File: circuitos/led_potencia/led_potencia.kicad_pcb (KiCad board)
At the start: 2 copper layers, 88.7 x 115.2 mm, 67 parts, among them J1 Conn_01x02_Pin, J10 Conn_01x02_Pin, J11 Conn_01x02_Pin, J12 Conn_01x02_Pin, J13 Conn_01x02_Pin, J14 Conn_01x02_Pin, J15 Conn_01x02_Pin, J16 Conn_01x02_Pin, J17 Conn_01x02_Socket, J19 Conn_01x02_OE_GND, J2 Conn_01x02_Pin, J20 Conn_01x05_IN, J21 Conn_01x05_OUT, J3 Conn_01x02_Pin, J4 Conn_01x02_Pin, J5 Conn_01x02_Pin, J6 Conn_01x02_Pin, J7 Conn_01x02_Pin, J8 Conn_01x02_Pin, J9 Conn_01x02_Pin, Q1 IRLZ44N, Q18 IRF4905, Q19 IRF4905, Q2 IRLZ44N, Q20 IRF4905, Q21 PN2222A, Q22 PN2222A, Q23 PN2222A, Q24 IRF4905, Q25 PN2222A, Q3 IRLZ44N, Q4 IRLZ44N, U1 74HC595

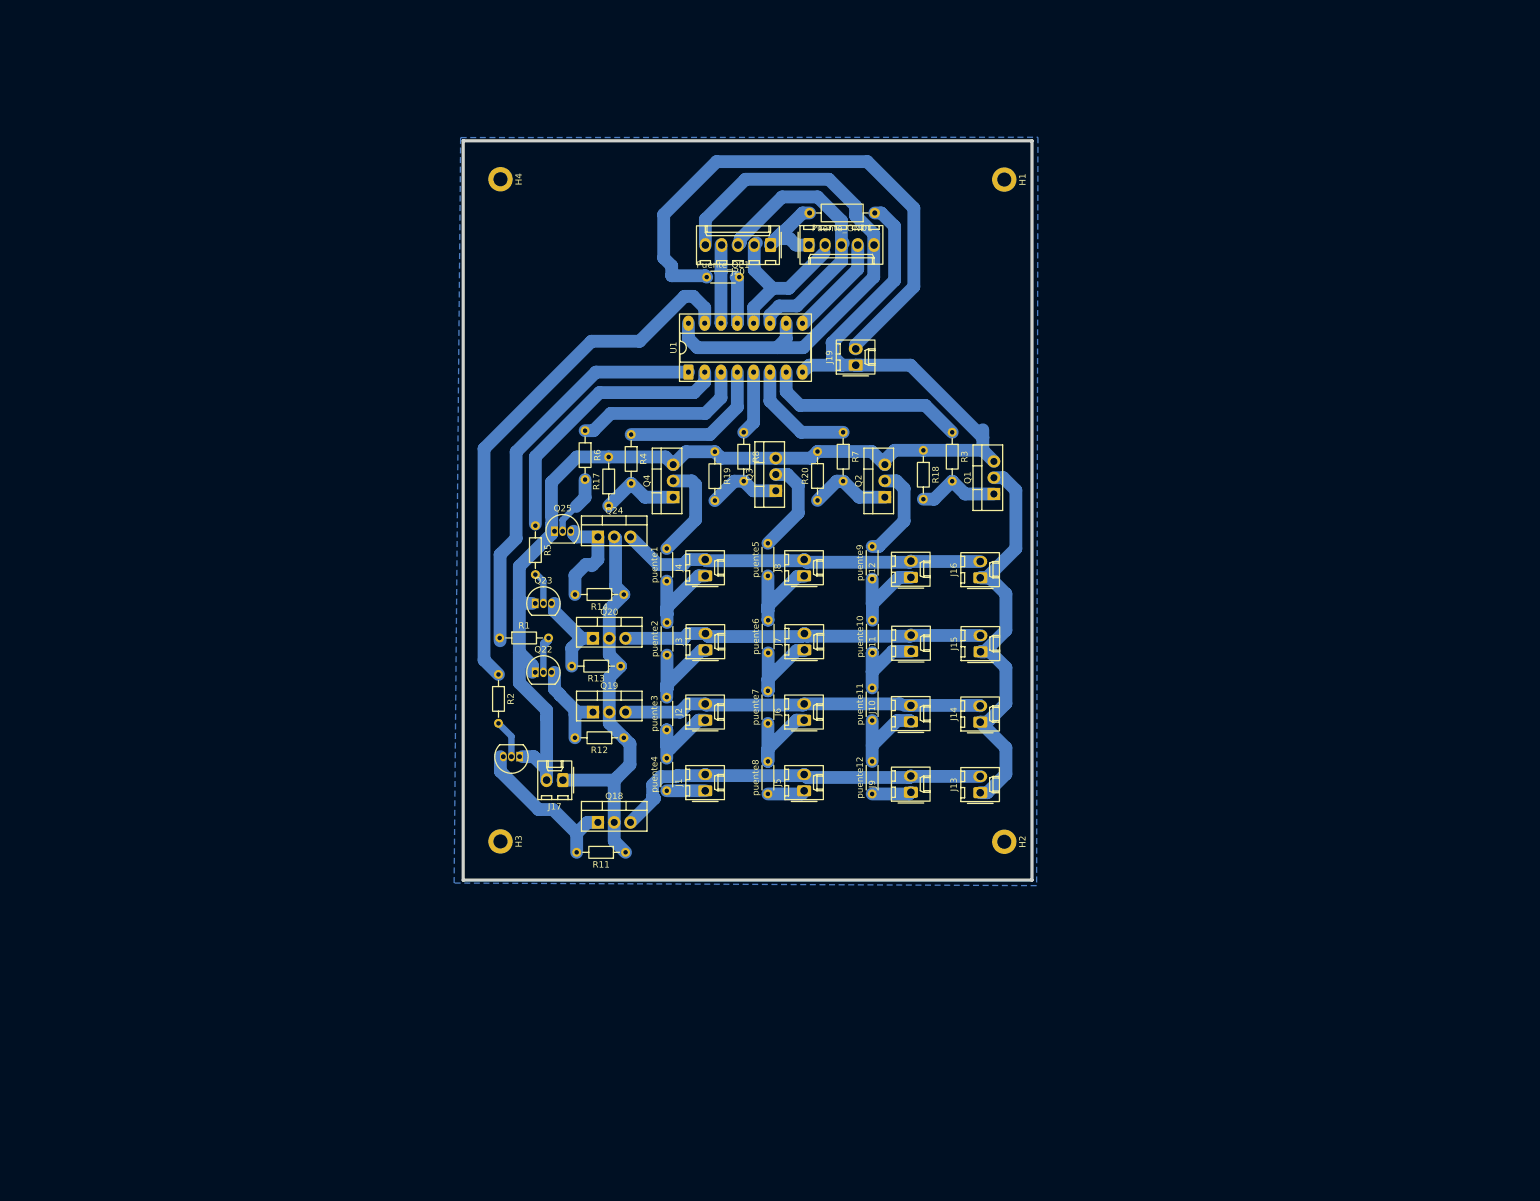
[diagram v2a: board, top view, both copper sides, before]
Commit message: cambios en ruteo
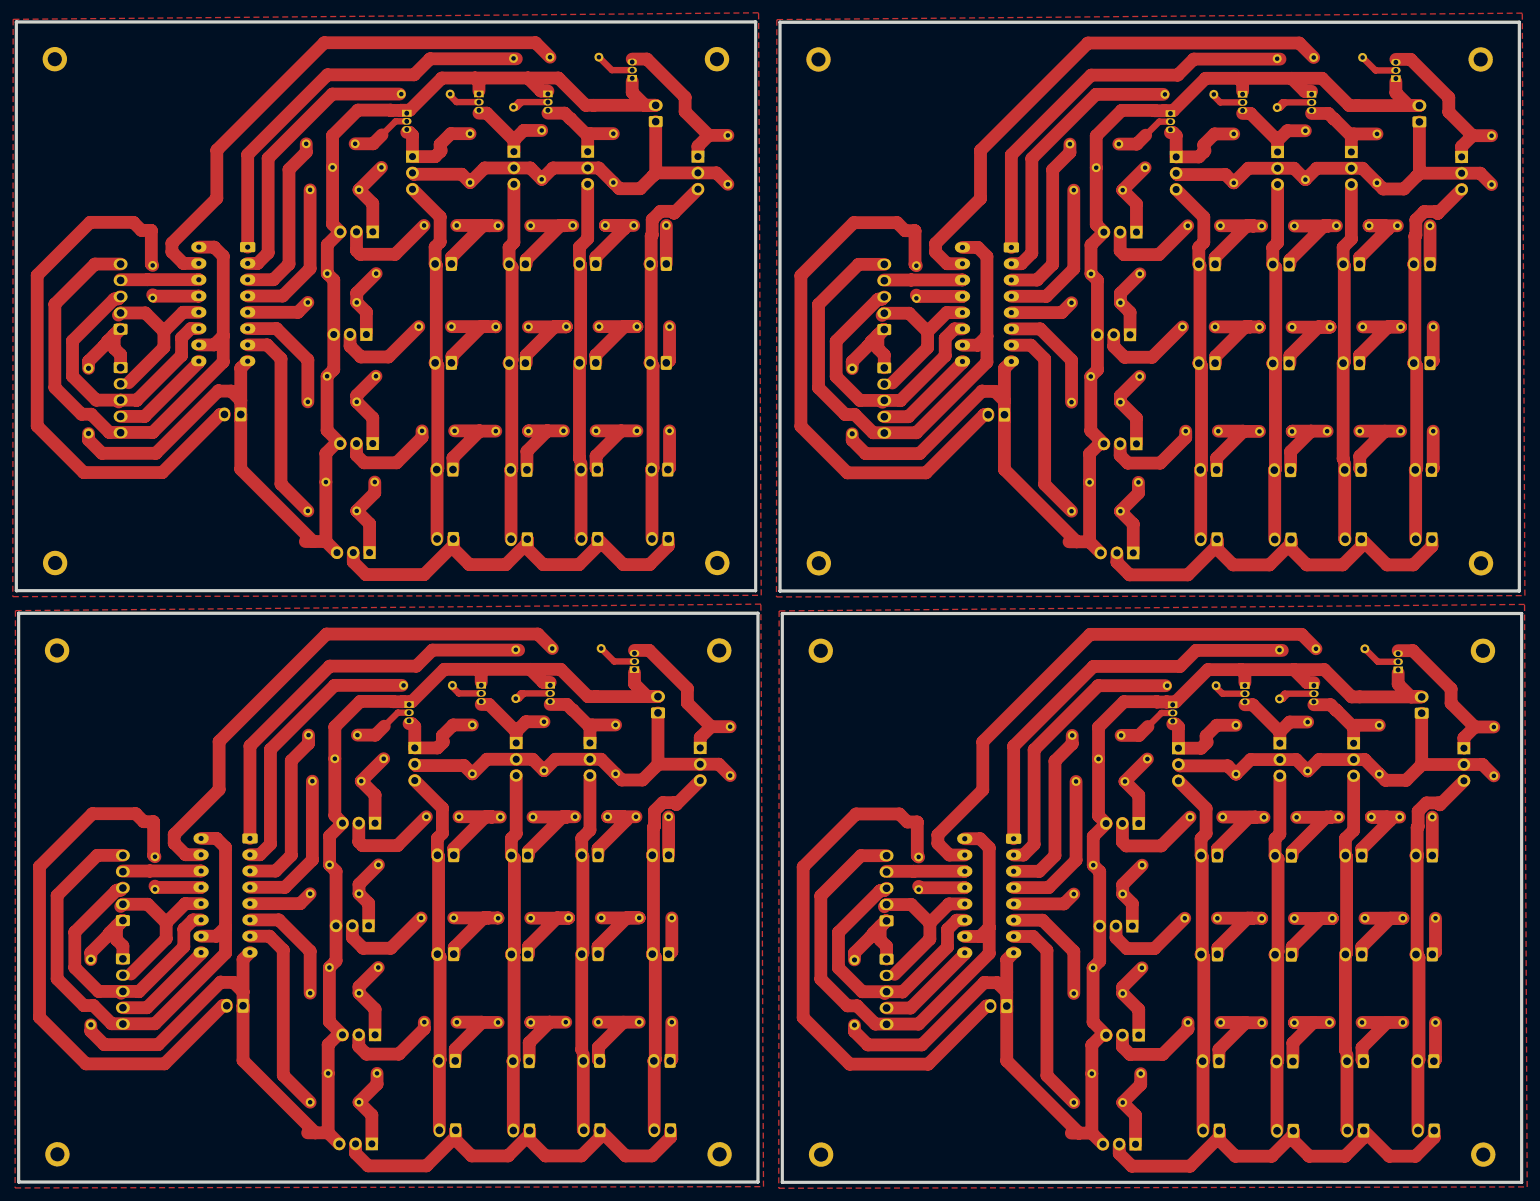
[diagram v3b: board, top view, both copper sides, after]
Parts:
- added H1: MountingHole, MountingHole:MountingHole_2.2mm_M2_DIN965_Pad, B.Cu at (142.8, 98.9)
- added H1: MountingHole, MountingHole:MountingHole_2.2mm_M2_DIN965_Pad, B.Cu at (143.2, 191.1)
- added H1: MountingHole, MountingHole:MountingHole_2.2mm_M2_DIN965_Pad, B.Cu at (23.8, 98.9)
- added H2: MountingHole, MountingHole:MountingHole_2.2mm_M2_DIN965_Pad, B.Cu at (246.1, 98.9)
- added H2: MountingHole, MountingHole:MountingHole_2.2mm_M2_DIN965_Pad, B.Cu at (246.4, 191.1)
- added H2: MountingHole, MountingHole:MountingHole_2.2mm_M2_DIN965_Pad, B.Cu at (127.0, 98.9)
- added H3: MountingHole, MountingHole:MountingHole_2.2mm_M2_DIN965_Pad, B.Cu at (246.4, 112.6)
- added H3: MountingHole, MountingHole:MountingHole_2.2mm_M2_DIN965_Pad, B.Cu at (246.0, 20.4)
- added H3: MountingHole, MountingHole:MountingHole_2.2mm_M2_DIN965_Pad, B.Cu at (127.0, 20.4)
- added H4: MountingHole, MountingHole:MountingHole_2.2mm_M2_DIN965_Pad, B.Cu at (23.7, 20.4)
- added H4: MountingHole, MountingHole:MountingHole_2.2mm_M2_DIN965_Pad, B.Cu at (143.1, 112.6)
- added H4: MountingHole, MountingHole:MountingHole_2.2mm_M2_DIN965_Pad, B.Cu at (142.8, 20.4)
- added J1: Conn_01x02_Pin, Connector_Molex:Molex_KK-254_AE-6410-02A_1x02_P2.54mm_Vertical, B.Cu at (119.1, 52.3)
- added J1: Conn_01x02_Pin, Connector_Molex:Molex_KK-254_AE-6410-02A_1x02_P2.54mm_Vertical, B.Cu at (238.5, 144.5)
- added J1: Conn_01x02_Pin, Connector_Molex:Molex_KK-254_AE-6410-02A_1x02_P2.54mm_Vertical, B.Cu at (238.1, 52.3)
- added J10: Conn_01x02_Pin, Connector_Molex:Molex_KK-254_AE-6410-02A_1x02_P2.54mm_Vertical, B.Cu at (108.3, 84.3)
- added J10: Conn_01x02_Pin, Connector_Molex:Molex_KK-254_AE-6410-02A_1x02_P2.54mm_Vertical, B.Cu at (227.7, 176.6)
- added J10: Conn_01x02_Pin, Connector_Molex:Molex_KK-254_AE-6410-02A_1x02_P2.54mm_Vertical, B.Cu at (227.3, 84.4)
- added J11: Conn_01x02_Pin, Connector_Molex:Molex_KK-254_AE-6410-02A_1x02_P2.54mm_Vertical, B.Cu at (97.3, 84.4)
- added J11: Conn_01x02_Pin, Connector_Molex:Molex_KK-254_AE-6410-02A_1x02_P2.54mm_Vertical, B.Cu at (216.4, 84.4)
- added J11: Conn_01x02_Pin, Connector_Molex:Molex_KK-254_AE-6410-02A_1x02_P2.54mm_Vertical, B.Cu at (216.7, 176.6)
- added J12: Conn_01x02_Pin, Connector_Molex:Molex_KK-254_AE-6410-02A_1x02_P2.54mm_Vertical, B.Cu at (85.8, 84.3)
- added J12: Conn_01x02_Pin, Connector_Molex:Molex_KK-254_AE-6410-02A_1x02_P2.54mm_Vertical, B.Cu at (205.2, 176.6)
- added J12: Conn_01x02_Pin, Connector_Molex:Molex_KK-254_AE-6410-02A_1x02_P2.54mm_Vertical, B.Cu at (204.8, 84.4)
- added J13: Conn_01x02_Pin, Connector_Molex:Molex_KK-254_AE-6410-02A_1x02_P2.54mm_Vertical, B.Cu at (238.8, 187.4)
- added J13: Conn_01x02_Pin, Connector_Molex:Molex_KK-254_AE-6410-02A_1x02_P2.54mm_Vertical, B.Cu at (119.4, 95.2)
- added J13: Conn_01x02_Pin, Connector_Molex:Molex_KK-254_AE-6410-02A_1x02_P2.54mm_Vertical, B.Cu at (238.4, 95.2)
- added J14: Conn_01x02_Pin, Connector_Molex:Molex_KK-254_AE-6410-02A_1x02_P2.54mm_Vertical, B.Cu at (227.8, 187.4)
- added J14: Conn_01x02_Pin, Connector_Molex:Molex_KK-254_AE-6410-02A_1x02_P2.54mm_Vertical, B.Cu at (227.4, 95.2)
- added J14: Conn_01x02_Pin, Connector_Molex:Molex_KK-254_AE-6410-02A_1x02_P2.54mm_Vertical, B.Cu at (108.4, 95.2)
- added J15: Conn_01x02_Pin, Connector_Molex:Molex_KK-254_AE-6410-02A_1x02_P2.54mm_Vertical, B.Cu at (216.8, 187.4)
- added J15: Conn_01x02_Pin, Connector_Molex:Molex_KK-254_AE-6410-02A_1x02_P2.54mm_Vertical, B.Cu at (216.4, 95.2)
- added J15: Conn_01x02_Pin, Connector_Molex:Molex_KK-254_AE-6410-02A_1x02_P2.54mm_Vertical, B.Cu at (97.4, 95.2)
- added J16: Conn_01x02_Pin, Connector_Molex:Molex_KK-254_AE-6410-02A_1x02_P2.54mm_Vertical, B.Cu at (205.3, 187.4)
- added J16: Conn_01x02_Pin, Connector_Molex:Molex_KK-254_AE-6410-02A_1x02_P2.54mm_Vertical, B.Cu at (204.9, 95.2)
- added J16: Conn_01x02_Pin, Connector_Molex:Molex_KK-254_AE-6410-02A_1x02_P2.54mm_Vertical, B.Cu at (85.9, 95.2)
- added J17: Conn_01x02_Socket, Connector_Molex:Molex_KK-254_AE-6410-02A_1x02_P2.54mm_Vertical, B.Cu at (236.4, 30.1)
- added J17: Conn_01x02_Socket, Connector_Molex:Molex_KK-254_AE-6410-02A_1x02_P2.54mm_Vertical, B.Cu at (117.4, 30.1)
- added J17: Conn_01x02_Socket, Connector_Molex:Molex_KK-254_AE-6410-02A_1x02_P2.54mm_Vertical, B.Cu at (236.8, 122.3)
- added J19: Conn_01x02_OE_GND, Connector_Molex:Molex_KK-254_AE-6410-02A_1x02_P2.54mm_Vertical, B.Cu at (172.1, 168.0)
- added J19: Conn_01x02_OE_GND, Connector_Molex:Molex_KK-254_AE-6410-02A_1x02_P2.54mm_Vertical, B.Cu at (52.7, 75.7)
- added J19: Conn_01x02_OE_GND, Connector_Molex:Molex_KK-254_AE-6410-02A_1x02_P2.54mm_Vertical, B.Cu at (171.8, 75.8)
- added J2: Conn_01x02_Pin, Connector_Molex:Molex_KK-254_AE-6410-02A_1x02_P2.54mm_Vertical, B.Cu at (227.5, 144.5)
- added J2: Conn_01x02_Pin, Connector_Molex:Molex_KK-254_AE-6410-02A_1x02_P2.54mm_Vertical, B.Cu at (108.1, 52.3)
- added J2: Conn_01x02_Pin, Connector_Molex:Molex_KK-254_AE-6410-02A_1x02_P2.54mm_Vertical, B.Cu at (227.1, 52.3)
- added J20: Conn_01x05_IN, Connector_Molex:Molex_KK-254_AE-6410-05A_1x05_P2.54mm_Vertical, B.Cu at (153.4, 154.7)
- added J20: Conn_01x05_IN, Connector_Molex:Molex_KK-254_AE-6410-05A_1x05_P2.54mm_Vertical, B.Cu at (34.0, 62.5)
- added J20: Conn_01x05_IN, Connector_Molex:Molex_KK-254_AE-6410-05A_1x05_P2.54mm_Vertical, B.Cu at (153.0, 62.5)
- added J21: Conn_01x05_OUT, Connector_Molex:Molex_KK-254_AE-6410-05A_1x05_P2.54mm_Vertical, B.Cu at (153.0, 68.5)
- added J21: Conn_01x05_OUT, Connector_Molex:Molex_KK-254_AE-6410-05A_1x05_P2.54mm_Vertical, B.Cu at (34.0, 68.4)
- added J21: Conn_01x05_OUT, Connector_Molex:Molex_KK-254_AE-6410-05A_1x05_P2.54mm_Vertical, B.Cu at (153.4, 160.7)
- added J3: Conn_01x02_Pin, Connector_Molex:Molex_KK-254_AE-6410-02A_1x02_P2.54mm_Vertical, B.Cu at (216.1, 52.4)
- added J3: Conn_01x02_Pin, Connector_Molex:Molex_KK-254_AE-6410-02A_1x02_P2.54mm_Vertical, B.Cu at (216.5, 144.5)
- added J3: Conn_01x02_Pin, Connector_Molex:Molex_KK-254_AE-6410-02A_1x02_P2.54mm_Vertical, B.Cu at (97.1, 52.3)
- added J4: Conn_01x02_Pin, Connector_Molex:Molex_KK-254_AE-6410-02A_1x02_P2.54mm_Vertical, B.Cu at (204.6, 52.3)
- added J4: Conn_01x02_Pin, Connector_Molex:Molex_KK-254_AE-6410-02A_1x02_P2.54mm_Vertical, B.Cu at (85.6, 52.3)
- added J4: Conn_01x02_Pin, Connector_Molex:Molex_KK-254_AE-6410-02A_1x02_P2.54mm_Vertical, B.Cu at (205.0, 144.5)
- added J5: Conn_01x02_Pin, Connector_Molex:Molex_KK-254_AE-6410-02A_1x02_P2.54mm_Vertical, B.Cu at (119.1, 67.7)
- added J5: Conn_01x02_Pin, Connector_Molex:Molex_KK-254_AE-6410-02A_1x02_P2.54mm_Vertical, B.Cu at (238.5, 159.9)
- added J5: Conn_01x02_Pin, Connector_Molex:Molex_KK-254_AE-6410-02A_1x02_P2.54mm_Vertical, B.Cu at (238.1, 67.8)
- added J6: Conn_01x02_Pin, Connector_Molex:Molex_KK-254_AE-6410-02A_1x02_P2.54mm_Vertical, B.Cu at (227.1, 67.8)
- added J6: Conn_01x02_Pin, Connector_Molex:Molex_KK-254_AE-6410-02A_1x02_P2.54mm_Vertical, B.Cu at (227.5, 159.9)
- added J6: Conn_01x02_Pin, Connector_Molex:Molex_KK-254_AE-6410-02A_1x02_P2.54mm_Vertical, B.Cu at (108.1, 67.7)
- added J7: Conn_01x02_Pin, Connector_Molex:Molex_KK-254_AE-6410-02A_1x02_P2.54mm_Vertical, B.Cu at (97.1, 67.7)
- added J7: Conn_01x02_Pin, Connector_Molex:Molex_KK-254_AE-6410-02A_1x02_P2.54mm_Vertical, B.Cu at (216.5, 160.0)
- added J7: Conn_01x02_Pin, Connector_Molex:Molex_KK-254_AE-6410-02A_1x02_P2.54mm_Vertical, B.Cu at (216.1, 67.8)
- added J8: Conn_01x02_Pin, Connector_Molex:Molex_KK-254_AE-6410-02A_1x02_P2.54mm_Vertical, B.Cu at (205.0, 159.9)
- added J8: Conn_01x02_Pin, Connector_Molex:Molex_KK-254_AE-6410-02A_1x02_P2.54mm_Vertical, B.Cu at (204.6, 67.8)
- added J8: Conn_01x02_Pin, Connector_Molex:Molex_KK-254_AE-6410-02A_1x02_P2.54mm_Vertical, B.Cu at (85.6, 67.7)
- added J9: Conn_01x02_Pin, Connector_Molex:Molex_KK-254_AE-6410-02A_1x02_P2.54mm_Vertical, B.Cu at (119.3, 84.3)
- added J9: Conn_01x02_Pin, Connector_Molex:Molex_KK-254_AE-6410-02A_1x02_P2.54mm_Vertical, B.Cu at (238.7, 176.6)
- added J9: Conn_01x02_Pin, Connector_Molex:Molex_KK-254_AE-6410-02A_1x02_P2.54mm_Vertical, B.Cu at (238.3, 84.4)
- added Puente_GND1: 0, Resistor_THT:R_Axial_DIN0207_L6.3mm_D2.5mm_P10.16mm_Horizontal, B.Cu at (148.4, 170.9)
- added Puente_GND1: 0, Resistor_THT:R_Axial_DIN0207_L6.3mm_D2.5mm_P10.16mm_Horizontal, B.Cu at (29.0, 78.7)
- added Puente_GND1: 0, Resistor_THT:R_Axial_DIN0207_L6.3mm_D2.5mm_P10.16mm_Horizontal, B.Cu at (148.0, 78.8)
- added Puente_OE1: 0, Resistor_THT:R_Axial_DIN0204_L3.6mm_D1.6mm_P5.08mm_Horizontal, B.Cu at (158.0, 52.6)
- added Puente_OE1: 0, Resistor_THT:R_Axial_DIN0204_L3.6mm_D1.6mm_P5.08mm_Horizontal, B.Cu at (39.0, 52.5)
- added Puente_OE1: 0, Resistor_THT:R_Axial_DIN0204_L3.6mm_D1.6mm_P5.08mm_Horizontal, B.Cu at (158.4, 144.7)
- added Q1: IRLZ44N, Package_TO_SOT_THT:TO-220-3_Vertical, B.Cu at (72.8, 97.3)
- added Q1: IRLZ44N, Package_TO_SOT_THT:TO-220-3_Vertical, B.Cu at (191.8, 97.3)
- added Q1: IRLZ44N, Package_TO_SOT_THT:TO-220-3_Vertical, B.Cu at (192.2, 189.5)
- added Q18: IRF4905, Package_TO_SOT_THT:TO-220-3_Vertical, B.Cu at (243.0, 35.6)
- added Q18: IRF4905, Package_TO_SOT_THT:TO-220-3_Vertical, B.Cu at (243.4, 127.8)
- added Q18: IRF4905, Package_TO_SOT_THT:TO-220-3_Vertical, B.Cu at (124.0, 35.6)
- added Q19: IRF4905, Package_TO_SOT_THT:TO-220-3_Vertical, B.Cu at (226.2, 127.0)
- added Q19: IRF4905, Package_TO_SOT_THT:TO-220-3_Vertical, B.Cu at (225.8, 34.8)
- added Q19: IRF4905, Package_TO_SOT_THT:TO-220-3_Vertical, B.Cu at (106.8, 34.8)
- added Q2: IRLZ44N, Package_TO_SOT_THT:TO-220-3_Vertical, B.Cu at (192.7, 172.5)
- added Q2: IRLZ44N, Package_TO_SOT_THT:TO-220-3_Vertical, B.Cu at (73.3, 80.3)
- added Q2: IRLZ44N, Package_TO_SOT_THT:TO-220-3_Vertical, B.Cu at (192.3, 80.3)
- added Q20: IRF4905, Package_TO_SOT_THT:TO-220-3_Vertical, B.Cu at (95.3, 34.8)
- added Q20: IRF4905, Package_TO_SOT_THT:TO-220-3_Vertical, B.Cu at (214.3, 34.8)
- added Q20: IRF4905, Package_TO_SOT_THT:TO-220-3_Vertical, B.Cu at (214.7, 127.0)
- added Q21: PN2222A, Package_TO_SOT_THT:TO-92_Inline, B.Cu at (113.7, 23.3)
- added Q21: PN2222A, Package_TO_SOT_THT:TO-92_Inline, B.Cu at (232.8, 23.4)
- added Q21: PN2222A, Package_TO_SOT_THT:TO-92_Inline, B.Cu at (233.1, 115.6)
- added Q22: PN2222A, Package_TO_SOT_THT:TO-92_Inline, B.Cu at (100.6, 25.8)
- added Q22: PN2222A, Package_TO_SOT_THT:TO-92_Inline, B.Cu at (220.0, 118.0)
- added Q22: PN2222A, Package_TO_SOT_THT:TO-92_Inline, B.Cu at (219.6, 25.8)
- added Q23: PN2222A, Package_TO_SOT_THT:TO-92_Inline, B.Cu at (209.2, 118.0)
- added Q23: PN2222A, Package_TO_SOT_THT:TO-92_Inline, B.Cu at (89.8, 25.8)
- added Q23: PN2222A, Package_TO_SOT_THT:TO-92_Inline, B.Cu at (208.9, 25.8)
- added Q24: IRF4905, Package_TO_SOT_THT:TO-220-3_Vertical, B.Cu at (198.9, 127.8)
- added Q24: IRF4905, Package_TO_SOT_THT:TO-220-3_Vertical, B.Cu at (79.5, 35.6)
- added Q24: IRF4905, Package_TO_SOT_THT:TO-220-3_Vertical, B.Cu at (198.5, 35.6)
- added Q25: PN2222A, Package_TO_SOT_THT:TO-92_Inline, B.Cu at (197.6, 28.8)
- added Q25: PN2222A, Package_TO_SOT_THT:TO-92_Inline, B.Cu at (78.6, 28.8)
- added Q25: PN2222A, Package_TO_SOT_THT:TO-92_Inline, B.Cu at (198.0, 121.0)
- added Q3: IRLZ44N, Package_TO_SOT_THT:TO-220-3_Vertical, B.Cu at (72.3, 63.3)
- added Q3: IRLZ44N, Package_TO_SOT_THT:TO-220-3_Vertical, B.Cu at (191.3, 63.3)
- added Q3: IRLZ44N, Package_TO_SOT_THT:TO-220-3_Vertical, B.Cu at (191.7, 155.5)
- added Q4: IRLZ44N, Package_TO_SOT_THT:TO-220-3_Vertical, B.Cu at (192.7, 139.5)
- added Q4: IRLZ44N, Package_TO_SOT_THT:TO-220-3_Vertical, B.Cu at (73.3, 47.3)
- added Q4: IRLZ44N, Package_TO_SOT_THT:TO-220-3_Vertical, B.Cu at (192.3, 47.3)
- added R1: 1k, Resistor_THT:R_Axial_DIN0204_L3.6mm_D1.6mm_P7.62mm_Horizontal, B.Cu at (214.6, 112.5)
- added R1: 1k, Resistor_THT:R_Axial_DIN0204_L3.6mm_D1.6mm_P7.62mm_Horizontal, B.Cu at (95.2, 20.2)
- added R1: 1k, Resistor_THT:R_Axial_DIN0204_L3.6mm_D1.6mm_P7.62mm_Horizontal, B.Cu at (214.3, 20.3)
- added R11: 10k, Resistor_THT:R_Axial_DIN0204_L3.6mm_D1.6mm_P7.62mm_Horizontal, B.Cu at (128.7, 39.9)
- added R11: 10k, Resistor_THT:R_Axial_DIN0204_L3.6mm_D1.6mm_P7.62mm_Horizontal, B.Cu at (248.1, 132.1)
- added R11: 10k, Resistor_THT:R_Axial_DIN0204_L3.6mm_D1.6mm_P7.62mm_Horizontal, B.Cu at (247.7, 39.9)
- added R12: 10k, Resistor_THT:R_Axial_DIN0204_L3.6mm_D1.6mm_P7.62mm_Horizontal, B.Cu at (229.8, 39.6)
- added R12: 10k, Resistor_THT:R_Axial_DIN0204_L3.6mm_D1.6mm_P7.62mm_Horizontal, B.Cu at (110.8, 39.6)
- added R12: 10k, Resistor_THT:R_Axial_DIN0204_L3.6mm_D1.6mm_P7.62mm_Horizontal, B.Cu at (230.2, 131.8)
- added R13: 10k, Resistor_THT:R_Axial_DIN0204_L3.6mm_D1.6mm_P7.62mm_Horizontal, B.Cu at (99.6, 39.1)
- added R13: 10k, Resistor_THT:R_Axial_DIN0204_L3.6mm_D1.6mm_P7.62mm_Horizontal, B.Cu at (219.0, 131.3)
- added R13: 10k, Resistor_THT:R_Axial_DIN0204_L3.6mm_D1.6mm_P7.62mm_Horizontal, B.Cu at (218.7, 39.1)
- added R14: 10k, Resistor_THT:R_Axial_DIN0204_L3.6mm_D1.6mm_P7.62mm_Horizontal, B.Cu at (88.5, 39.6)
- added R14: 10k, Resistor_THT:R_Axial_DIN0204_L3.6mm_D1.6mm_P7.62mm_Horizontal, B.Cu at (207.9, 131.8)
- added R14: 10k, Resistor_THT:R_Axial_DIN0204_L3.6mm_D1.6mm_P7.62mm_Horizontal, B.Cu at (207.5, 39.6)
- added R17: 10k, Resistor_THT:R_Axial_DIN0204_L3.6mm_D1.6mm_P7.62mm_Horizontal, B.Cu at (74.6, 37.2)
- added R17: 10k, Resistor_THT:R_Axial_DIN0204_L3.6mm_D1.6mm_P7.62mm_Horizontal, B.Cu at (193.7, 37.3)
- added R17: 10k, Resistor_THT:R_Axial_DIN0204_L3.6mm_D1.6mm_P7.62mm_Horizontal, B.Cu at (194.1, 129.5)
- added R18: 10k, Resistor_THT:R_Axial_DIN0204_L3.6mm_D1.6mm_P7.62mm_Horizontal, B.Cu at (66.0, 86.3)
- added R18: 10k, Resistor_THT:R_Axial_DIN0204_L3.6mm_D1.6mm_P7.62mm_Horizontal, B.Cu at (185.0, 86.3)
- added R18: 10k, Resistor_THT:R_Axial_DIN0204_L3.6mm_D1.6mm_P7.62mm_Horizontal, B.Cu at (185.4, 178.5)
- added R19: 10k, Resistor_THT:R_Axial_DIN0204_L3.6mm_D1.6mm_P7.62mm_Horizontal, B.Cu at (66.2, 53.8)
- added R19: 10k, Resistor_THT:R_Axial_DIN0204_L3.6mm_D1.6mm_P7.62mm_Horizontal, B.Cu at (185.3, 53.8)
- added R19: 10k, Resistor_THT:R_Axial_DIN0204_L3.6mm_D1.6mm_P7.62mm_Horizontal, B.Cu at (185.6, 146.0)
- added R2: 1k, Resistor_THT:R_Axial_DIN0204_L3.6mm_D1.6mm_P7.62mm_Horizontal, B.Cu at (220.3, 112.3)
- added R2: 1k, Resistor_THT:R_Axial_DIN0204_L3.6mm_D1.6mm_P7.62mm_Horizontal, B.Cu at (100.9, 20.1)
- added R2: 1k, Resistor_THT:R_Axial_DIN0204_L3.6mm_D1.6mm_P7.62mm_Horizontal, B.Cu at (220.0, 20.1)
- added R20: 10k, Resistor_THT:R_Axial_DIN0204_L3.6mm_D1.6mm_P7.62mm_Horizontal, B.Cu at (73.8, 69.8)
- added R20: 10k, Resistor_THT:R_Axial_DIN0204_L3.6mm_D1.6mm_P7.62mm_Horizontal, B.Cu at (192.8, 69.8)
- added R20: 10k, Resistor_THT:R_Axial_DIN0204_L3.6mm_D1.6mm_P7.62mm_Horizontal, B.Cu at (193.2, 162.0)
- added R3: 1k, Resistor_THT:R_Axial_DIN0204_L3.6mm_D1.6mm_P7.62mm_Horizontal, B.Cu at (182.6, 183.0)
- added R3: 1k, Resistor_THT:R_Axial_DIN0204_L3.6mm_D1.6mm_P7.62mm_Horizontal, B.Cu at (63.2, 90.8)
- added R3: 1k, Resistor_THT:R_Axial_DIN0204_L3.6mm_D1.6mm_P7.62mm_Horizontal, B.Cu at (182.2, 90.8)
- added R4: 1k, Resistor_THT:R_Axial_DIN0204_L3.6mm_D1.6mm_P7.62mm_Horizontal, B.Cu at (63.5, 40.7)
- added R4: 1k, Resistor_THT:R_Axial_DIN0204_L3.6mm_D1.6mm_P7.62mm_Horizontal, B.Cu at (182.9, 133.0)
- added R4: 1k, Resistor_THT:R_Axial_DIN0204_L3.6mm_D1.6mm_P7.62mm_Horizontal, B.Cu at (182.6, 40.8)
- added R5: 1k, Resistor_THT:R_Axial_DIN0204_L3.6mm_D1.6mm_P7.62mm_Horizontal, B.Cu at (197.1, 118.0)
- added R5: 1k, Resistor_THT:R_Axial_DIN0204_L3.6mm_D1.6mm_P7.62mm_Horizontal, B.Cu at (77.7, 25.8)
- added R5: 1k, Resistor_THT:R_Axial_DIN0204_L3.6mm_D1.6mm_P7.62mm_Horizontal, B.Cu at (196.8, 25.9)
- added R6: 1k, Resistor_THT:R_Axial_DIN0204_L3.6mm_D1.6mm_P7.62mm_Horizontal, B.Cu at (182.3, 125.8)
- added R6: 1k, Resistor_THT:R_Axial_DIN0204_L3.6mm_D1.6mm_P7.62mm_Horizontal, B.Cu at (182.0, 33.6)
- added R6: 1k, Resistor_THT:R_Axial_DIN0204_L3.6mm_D1.6mm_P7.62mm_Horizontal, B.Cu at (62.9, 33.6)
- added R7: 1k, Resistor_THT:R_Axial_DIN0204_L3.6mm_D1.6mm_P7.62mm_Horizontal, B.Cu at (182.6, 166.0)
- added R7: 1k, Resistor_THT:R_Axial_DIN0204_L3.6mm_D1.6mm_P7.62mm_Horizontal, B.Cu at (63.2, 73.8)
- added R7: 1k, Resistor_THT:R_Axial_DIN0204_L3.6mm_D1.6mm_P7.62mm_Horizontal, B.Cu at (182.2, 73.8)
- added R8: 1k, Resistor_THT:R_Axial_DIN0204_L3.6mm_D1.6mm_P7.62mm_Horizontal, B.Cu at (182.2, 58.3)
- added R8: 1k, Resistor_THT:R_Axial_DIN0204_L3.6mm_D1.6mm_P7.62mm_Horizontal, B.Cu at (63.2, 58.3)
- added R8: 1k, Resistor_THT:R_Axial_DIN0204_L3.6mm_D1.6mm_P7.62mm_Horizontal, B.Cu at (182.6, 150.5)
- added U1: 74HC595, Package_DIP:DIP-16_W7.62mm_Socket_LongPads, B.Cu at (53.8, 49.7)
- added U1: 74HC595, Package_DIP:DIP-16_W7.62mm_Socket_LongPads, B.Cu at (172.8, 49.7)
- added U1: 74HC595, Package_DIP:DIP-16_W7.62mm_Socket_LongPads, B.Cu at (173.2, 141.9)
- added puente1: 0, Resistor_THT:R_Axial_DIN0204_L3.6mm_D1.6mm_P5.08mm_Horizontal, B.Cu at (205.4, 46.3)
- added puente1: 0, Resistor_THT:R_Axial_DIN0204_L3.6mm_D1.6mm_P5.08mm_Horizontal, B.Cu at (86.4, 46.3)
- added puente1: 0, Resistor_THT:R_Axial_DIN0204_L3.6mm_D1.6mm_P5.08mm_Horizontal, B.Cu at (205.8, 138.5)
- added puente10: 0, Resistor_THT:R_Axial_DIN0204_L3.6mm_D1.6mm_P5.08mm_Horizontal, B.Cu at (97.6, 78.3)
- added puente10: 0, Resistor_THT:R_Axial_DIN0204_L3.6mm_D1.6mm_P5.08mm_Horizontal, B.Cu at (217.0, 170.6)
- added puente10: 0, Resistor_THT:R_Axial_DIN0204_L3.6mm_D1.6mm_P5.08mm_Horizontal, B.Cu at (216.6, 78.4)
- added puente11: 0, Resistor_THT:R_Axial_DIN0204_L3.6mm_D1.6mm_P5.08mm_Horizontal, B.Cu at (227.5, 170.5)
- added puente11: 0, Resistor_THT:R_Axial_DIN0204_L3.6mm_D1.6mm_P5.08mm_Horizontal, B.Cu at (108.1, 78.3)
- added puente11: 0, Resistor_THT:R_Axial_DIN0204_L3.6mm_D1.6mm_P5.08mm_Horizontal, B.Cu at (227.2, 78.4)
- added puente12: 0, Resistor_THT:R_Axial_DIN0204_L3.6mm_D1.6mm_P5.08mm_Horizontal, B.Cu at (238.6, 78.4)
- added puente12: 0, Resistor_THT:R_Axial_DIN0204_L3.6mm_D1.6mm_P5.08mm_Horizontal, B.Cu at (239.0, 170.5)
- added puente12: 0, Resistor_THT:R_Axial_DIN0204_L3.6mm_D1.6mm_P5.08mm_Horizontal, B.Cu at (119.6, 78.3)
- added puente2: 0, Resistor_THT:R_Axial_DIN0204_L3.6mm_D1.6mm_P5.08mm_Horizontal, B.Cu at (217.3, 138.5)
- added puente2: 0, Resistor_THT:R_Axial_DIN0204_L3.6mm_D1.6mm_P5.08mm_Horizontal, B.Cu at (217.0, 46.4)
- added puente2: 0, Resistor_THT:R_Axial_DIN0204_L3.6mm_D1.6mm_P5.08mm_Horizontal, B.Cu at (97.9, 46.3)
- added puente3: 0, Resistor_THT:R_Axial_DIN0204_L3.6mm_D1.6mm_P5.08mm_Horizontal, B.Cu at (228.6, 46.3)
- added puente3: 0, Resistor_THT:R_Axial_DIN0204_L3.6mm_D1.6mm_P5.08mm_Horizontal, B.Cu at (229.0, 138.5)
- added puente3: 0, Resistor_THT:R_Axial_DIN0204_L3.6mm_D1.6mm_P5.08mm_Horizontal, B.Cu at (109.6, 46.3)
- added puente4: 0, Resistor_THT:R_Axial_DIN0204_L3.6mm_D1.6mm_P5.08mm_Horizontal, B.Cu at (238.5, 138.5)
- added puente4: 0, Resistor_THT:R_Axial_DIN0204_L3.6mm_D1.6mm_P5.08mm_Horizontal, B.Cu at (238.1, 46.3)
- added puente4: 0, Resistor_THT:R_Axial_DIN0204_L3.6mm_D1.6mm_P5.08mm_Horizontal, B.Cu at (119.1, 46.3)
- added puente5: 0, Resistor_THT:R_Axial_DIN0204_L3.6mm_D1.6mm_P5.08mm_Horizontal, B.Cu at (204.6, 62.1)
- added puente5: 0, Resistor_THT:R_Axial_DIN0204_L3.6mm_D1.6mm_P5.08mm_Horizontal, B.Cu at (205.0, 154.3)
- added puente5: 0, Resistor_THT:R_Axial_DIN0204_L3.6mm_D1.6mm_P5.08mm_Horizontal, B.Cu at (85.6, 62.1)
- added puente6: 0, Resistor_THT:R_Axial_DIN0204_L3.6mm_D1.6mm_P5.08mm_Horizontal, B.Cu at (97.6, 62.1)
- added puente6: 0, Resistor_THT:R_Axial_DIN0204_L3.6mm_D1.6mm_P5.08mm_Horizontal, B.Cu at (216.6, 62.1)
- added puente6: 0, Resistor_THT:R_Axial_DIN0204_L3.6mm_D1.6mm_P5.08mm_Horizontal, B.Cu at (217.0, 154.3)
- added puente7: 0, Resistor_THT:R_Axial_DIN0204_L3.6mm_D1.6mm_P5.08mm_Horizontal, B.Cu at (227.6, 62.1)
- added puente7: 0, Resistor_THT:R_Axial_DIN0204_L3.6mm_D1.6mm_P5.08mm_Horizontal, B.Cu at (108.6, 62.1)
- added puente7: 0, Resistor_THT:R_Axial_DIN0204_L3.6mm_D1.6mm_P5.08mm_Horizontal, B.Cu at (228.0, 154.3)
- added puente8: 0, Resistor_THT:R_Axial_DIN0204_L3.6mm_D1.6mm_P5.08mm_Horizontal, B.Cu at (239.0, 154.3)
- added puente8: 0, Resistor_THT:R_Axial_DIN0204_L3.6mm_D1.6mm_P5.08mm_Horizontal, B.Cu at (238.6, 62.1)
- added puente8: 0, Resistor_THT:R_Axial_DIN0204_L3.6mm_D1.6mm_P5.08mm_Horizontal, B.Cu at (119.6, 62.1)
- added puente9: 0, Resistor_THT:R_Axial_DIN0204_L3.6mm_D1.6mm_P5.08mm_Horizontal, B.Cu at (205.1, 78.4)
- added puente9: 0, Resistor_THT:R_Axial_DIN0204_L3.6mm_D1.6mm_P5.08mm_Horizontal, B.Cu at (86.1, 78.3)
- added puente9: 0, Resistor_THT:R_Axial_DIN0204_L3.6mm_D1.6mm_P5.08mm_Horizontal, B.Cu at (205.5, 170.5)
- H1, H2, H3, H4, J1, J10, J11, J12, J13, J14, J15, J16, J17, J19, J2, J20, J21, J3, J4, J5, J6, J7, J8, J9, Puente_GND1, Puente_OE1, Q1, Q18, Q19, Q2, Q20, Q21, Q22, Q23, Q24, Q25, Q3, Q4, R1, R11, R12, R13, R14, R17, R18, R19, R2, R20, R3, R4, R5, R6, R7, R8, U1, puente1, puente10, puente11, puente12, puente2, puente3, puente4, puente5, puente6, puente7, puente8, puente9: moved to B.Cu
- moved H1 211.8 mm to (24.1, 191.1), turned to 0 degrees
- moved Puente_GND1 175.9 mm to (29.3, 170.9), turned to 90 degrees
- moved J21 154.3 mm to (34.3, 160.6), turned to -90 degrees
- moved J20 145.9 mm to (34.3, 154.6), turned to 90 degrees
- moved R3 144.7 mm to (63.5, 183.0), turned to 0 degrees
- moved Q1 140.2 mm to (73.2, 189.5), turned to 180 degrees
- moved J19 138.2 mm to (53.1, 167.9), turned to 180 degrees
- moved R18 134.3 mm to (66.3, 178.5), turned to 0 degrees
- moved Puente_OE1 124.7 mm to (39.3, 144.7), turned to -90 degrees
- moved R7 120.6 mm to (63.5, 166.0), turned to 0 degrees
- moved J16 118.8 mm to (86.2, 187.3), turned to 180 degrees
- moved Q2 115.5 mm to (73.7, 172.5), turned to 180 degrees
- moved J12 103.6 mm to (86.2, 176.5), turned to 180 degrees
- moved J15 102.5 mm to (97.7, 187.4), turned to 180 degrees
- moved H4 100.9 mm to (24.1, 112.5), turned to 0 degrees
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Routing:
- net GND: track 206.0 -> 823.8 mm
- net Net-(J19-Pin_2): track 86.7 -> 346.8 mm
- net VCC: track 84.8 -> 339.3 mm
- net Net-(U1-QA): track 83.5 -> 334.0 mm
- net Net-(J13-Pin_1): track 67.6 -> 270.3 mm
- net +12V: track 62.9 -> 251.5 mm
- net Net-(U1-QB): track 62.5 -> 250.0 mm
- net Net-(J1-Pin_2): track 59.7 -> 238.9 mm
- net Net-(J12-Pin_2): track 57.1 -> 228.2 mm
- net Net-(J11-Pin_2): track 56.3 -> 225.2 mm
- net Net-(J10-Pin_2): track 55.2 -> 221.0 mm
- net Net-(J20-Pin_3): track 43.8 -> 175.1 mm
- net Net-(U1-QC): track 43.3 -> 173.1 mm
- net Net-(U1-QH): track 31.5 -> 126.2 mm
- net Net-(U1-QD): track 27.3 -> 109.3 mm
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- added copper zone on F.Cu, net GND
- removed copper zone on B.Cu, net GND
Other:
- board size 88.7 x 115.2 mm -> 234.7 x 180.9 mm
